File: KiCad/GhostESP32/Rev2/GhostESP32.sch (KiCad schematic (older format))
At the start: 33 parts, among them J1 CONN_02X20, P1 USB_OTG, Q1 Q_NPN_BEC, Q2 Q_NPN_BEC, SW1 SW_SPDT, U1 LM358, U2 NCP1117ST33T3G, U3 CP2102, U4 ESP-WROOM-32

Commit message: Working on the Encoder
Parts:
- added R8, R9: 2k2, symbol R
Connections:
- net +3V3: now also R8.1, R9.1
- net +5V: now also J1.35 (P35), J1.36 (P36), J1.37 (P37), J1.38 (P38), J1.39 (P39), J1.40 (P40); no longer J1.27 (P27), J1.28 (P28), J1.29 (P29), J1.30 (P30)
- net IO13: now also J1.33 (P33); no longer J1.39 (P39)
- net IO14: now also J1.34 (P34); no longer J1.6 (P6)
- net IO16: now also J1.27 (P27); no longer J1.34 (P34)
- net IO17: now also J1.26 (P26); no longer J1.33 (P33)
- net IO18: now also J1.25 (P25); no longer J1.36 (P36)
- net IO19: now also J1.24 (P24); no longer J1.35 (P35)
- net IO21: now also J1.23 (P23); no longer J1.38 (P38)
- net IO22: now also J1.22 (P22); no longer J1.37 (P37)
- net IO23: now also J1.21 (P21); no longer J1.40 (P40)
- net IO25: now also J1.3 (P3); no longer J1.5 (P5)
- net IO27: now also J1.1 (P1); no longer J1.4 (P4)
- net IO32: now also J1.5 (P5), R9.2; no longer J1.1 (P1)
- net IO33: now also J1.4 (P4), R8.2; no longer J1.3 (P3)
- net IO4: now also J1.28 (P28); no longer J1.32 (P32)
- net IO2: now reaches U4.24 (IO2)
- no-connect marks 35 -> 31
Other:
- note added: "I2C pull-ups. \nOnly used when using \nboard in single-board mode."
- note added: "NB, GPIO_35 is Input only.\nGOIO_12 is Strapping pin."
- moved on the sheet: C10, C9, R10, R11, SW1

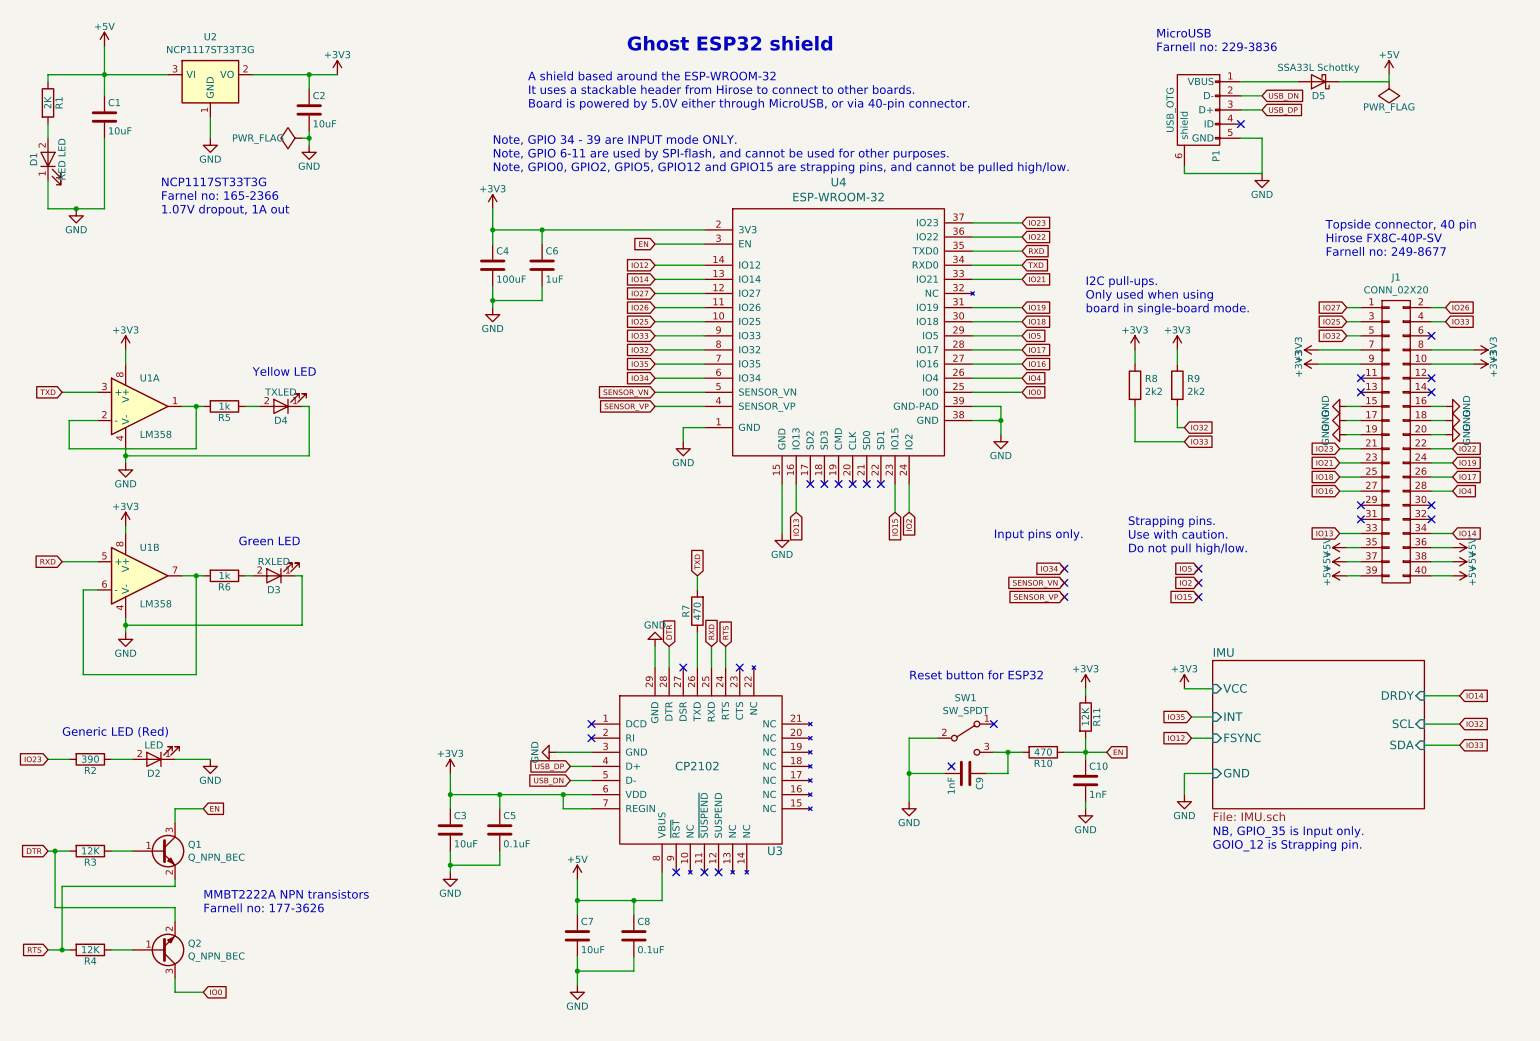
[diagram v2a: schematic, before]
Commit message: Ready to start routing. Schematics should be done.
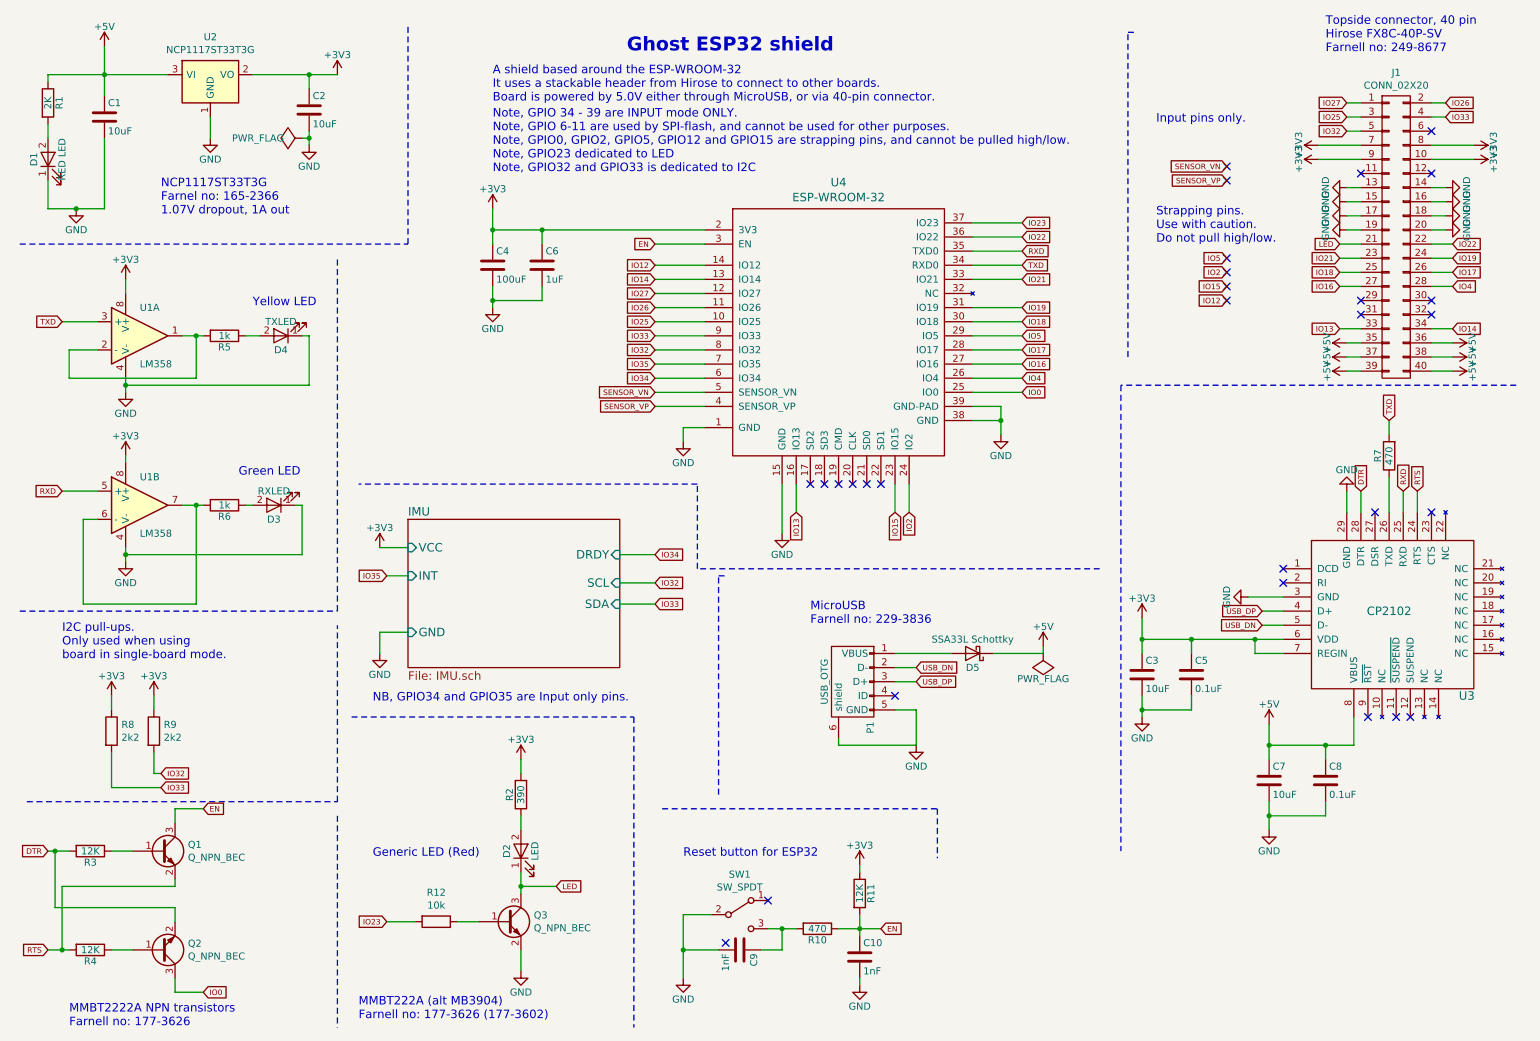
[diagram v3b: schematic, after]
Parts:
- added Q3: Q_NPN_BEC, TO_SOT_Packages_SMD:SOT-23, symbol Q_NPN_BEC
- added R12: 10k, Resistors_SMD:R_0603, symbol R
- R8, R9: footprint (none) -> Resistors_SMD:R_0603
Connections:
- net +3V3: now also R2.2
- net GND: now also J1.13 (P13), J1.14 (P14), Q3.2 (E); no longer D2.1 (K)
- net IO23: now also R12.2; no longer J1.21 (P21), R2.2
- new net: Q3.1 (B), R12.1
- new net LED: D2.1 (K), J1.21 (P21), Q3.3 (C)
- no-connect marks 31 -> 29
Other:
- note added: "MMBT222A (alt MB3904)\nFarnell no: 177-3626 (177-3602)"
- note added: "NB, GPIO34 and GPIO35 are Input only pins."
- note added: "Note, GPIO 34 - 39 are INPUT mode ONLY.\nNote, GPIO 6-11 are used by SPI-flash, and cannot be used for other purposes.\nNote, GPIO0, GPIO2, GPIO5, GPIO12 and GPIO15 are strapping pins, and cannot be pulled high/low.\nNote, GPIO23 dedicated to LED\nNote, GPIO32 and GPIO33 is dedicated to I2C"
- note removed: "NB, GPIO_35 is Input only.\nGOIO_12 is Strapping pin."
- note removed: "Note, GPIO 34 - 39 are INPUT mode ONLY.\nNote, GPIO 6-11 are used by SPI-flash, and cannot be used for other purposes.\nNote, GPIO0, GPIO2, GPIO5, GPIO12 and GPIO15 are strapping pins, and cannot be pulled high/low."
- moved on the sheet: C10, C3, C5, C7, C8, C9, D2, D3, D4, D5, J1, P1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

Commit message: Rev2 sent to Elecrow for production
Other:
- note added: "Reset button for ESP32\nFarnell no: 152-2053"
- note removed: "Reset button for ESP32"
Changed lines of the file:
@@
 	6350 7000 6650 7000
 Text Notes 5250 6500 0    60   ~ 0
-Reset button for ESP32
+Reset button for ESP32\nFarnell no: 152-2053
 NoConn ~ 10300 5500
 Text Notes 2100 3800 0    60   ~ 0

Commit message: Minor
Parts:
- C1, C10, C2, C3, C4, C5, C6, C7, C8, C9: symbol C -> GhostESP32-rescue:C-RESCUE-GhostESP32
- D1, D2, D3, D4: symbol LED -> GhostESP32-rescue:LED-RESCUE-GhostESP32
- D5: symbol D_Schottky -> GhostESP32-rescue:D_Schottky-RESCUE-GhostESP32
- J1: symbol CONN_02X20 -> GhostESP32-rescue:CONN_02X20-RESCUE-GhostESP32
- P1: symbol USB_OTG-RESCUE-GhostESP32 -> GhostESP32-rescue:USB_OTG-RESCUE-GhostESP32
- Q1, Q2, Q3: symbol Q_NPN_BEC -> GhostESP32-rescue:Q_NPN_BEC-RESCUE-GhostESP32
- R1, R10, R11, R12, R2, R3, R4, R5, R6, R7, R8, R9: symbol R -> GhostESP32-rescue:R-RESCUE-GhostESP32
- SW1: symbol SW_SPDT -> GhostESP32-rescue:SW_SPDT-RESCUE-GhostESP32
- U1: symbol LM358 -> GhostESP32-rescue:LM358-RESCUE-GhostESP32
- U2: symbol NCP1117ST33T3G -> GhostESP32-rescue:NCP1117ST33T3G-RESCUE-GhostESP32
- U3: symbol CP2102 -> NorBot:CP2102
- U4: symbol ESP-WROOM-32 -> GhostESP32-rescue:ESP-WROOM-32-RESCUE-GhostESP32
